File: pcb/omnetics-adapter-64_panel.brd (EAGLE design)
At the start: 119 x 83 mm, 87 parts, among them J1 DF40-REC, J10 DF40-REC, J13 DF40-REC, J16 DF40-REC, J19 DF40-REC, J22 DF40-REC, J25 DF40-REC, J4 DF40-REC, J7 DF40-REC

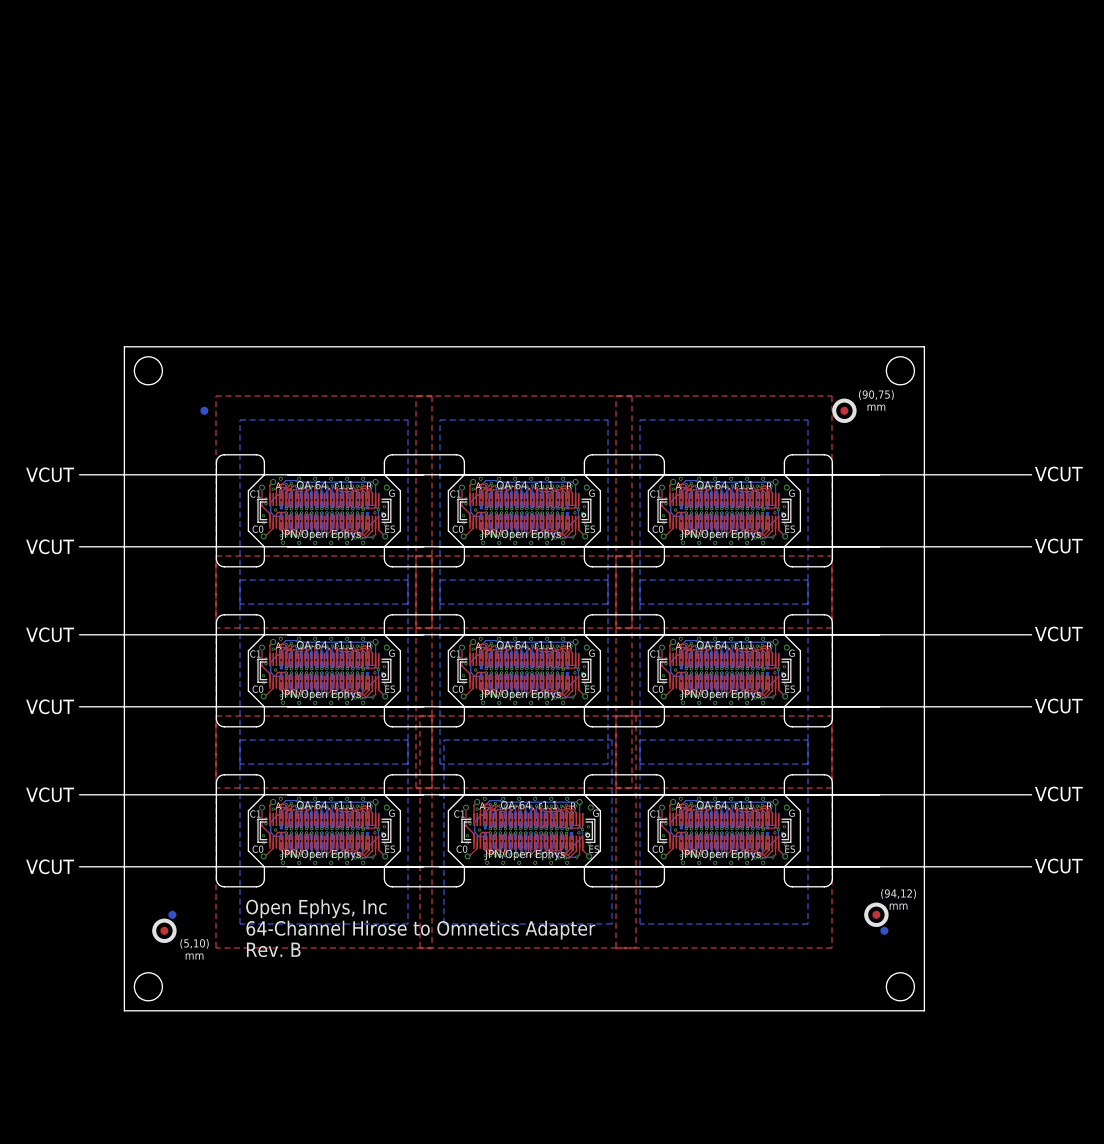
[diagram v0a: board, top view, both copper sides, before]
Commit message: Replace design with 1.3 pinout
- This pinout fits headstage-64 that is in the field
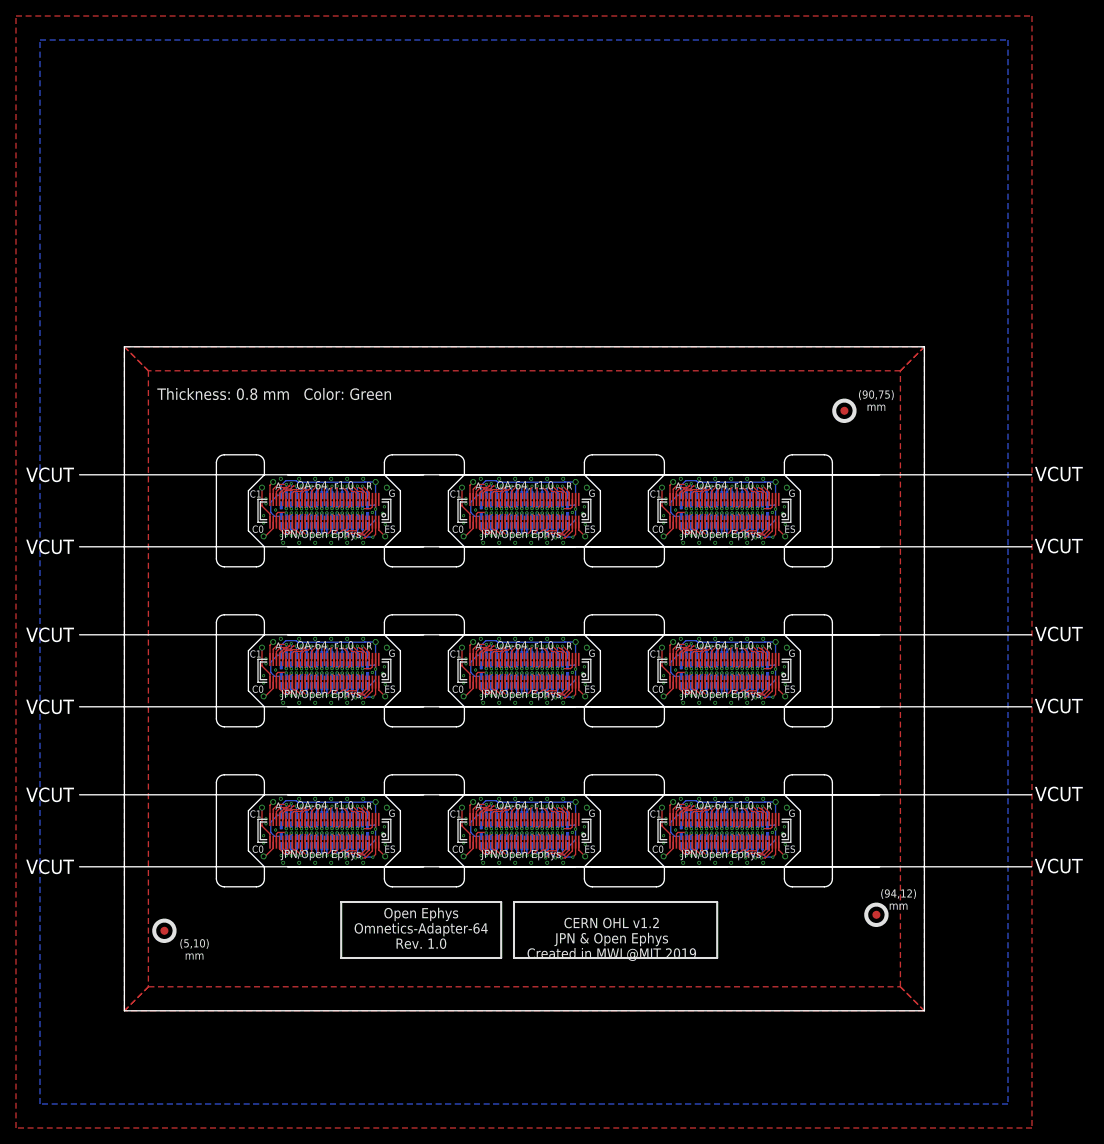
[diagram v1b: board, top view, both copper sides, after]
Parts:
- removed E$4, E$5, E$6: (no value), fiducial:FIDUCIAL
- moved CAT12 50.0 mm to (17.4, 59.3)
- moved CAT16 50.0 mm to (67.4, 59.3)
- moved ESTIM19 50.0 mm to (31.4, 66.1)
- moved ESTIM25 50.0 mm to (81.4, 66.1)
- moved CAT13 50.0 mm to (17.2, 65.4)
- moved CAT17 50.0 mm to (67.2, 65.4)
- moved ESTIM20 50.0 mm to (32.8, 65.4)
- moved ESTIM26 50.0 mm to (82.8, 65.4)
- moved J19 50.0 mm to (25.0, 62.5)
- moved J25 50.0 mm to (75.0, 62.5)
- moved AN6 50.0 mm to (18.6, 66.1)
- moved AN8 50.0 mm to (68.6, 66.1)
- moved ESTIM18 50.0 mm to (32.6, 59.3)
- moved ESTIM24 50.0 mm to (82.6, 59.3)
- moved J20 50.0 mm to (19.6, 64.5)
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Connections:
- removed net GND1: ESTIM2.P$1, J1.37, J2.18, J2.36, J3.18, J3.36
- removed net GND2: ESTIM8.P$1, J7.37, J8.18, J8.36, J9.18, J9.36
- removed net GND3: ESTIM11.P$1, J10.37, J11.18, J11.36, J12.18, J12.36
- removed net GND4: ESTIM14.P$1, J13.37, J14.18, J14.36, J15.18, J15.36
- removed net GND5: ESTIM17.P$1, J16.37, J17.18, J17.36, J18.18, J18.36
- removed net GND6: ESTIM20.P$1, J19.37, J20.18, J20.36, J21.18, J21.36
- removed net GND7: ESTIM23.P$1, J22.37, J23.18, J23.36, J24.18, J24.36
- removed net GND8: ESTIM26.P$1, J25.37, J26.18, J26.36, J27.18, J27.36
- net GND: now also ESTIM11.P$1, ESTIM14.P$1, ESTIM17.P$1, ESTIM2.P$1, ESTIM20.P$1, ESTIM23.P$1, ESTIM26.P$1, ESTIM8.P$1, J1.70, J10.70, J11.18, J11.36, J12.18, J12.36, J13.70, J14.18, J14.36, J15.18, J15.36, J16.70, J17.18, J17.36, J18.18, J18.36, J19.70, J2.18, J2.36, J20.18, J20.36, J21.18, J21.36, J22.70, J23.18, J23.36, J24.18, J24.36, J25.70, J26.18, J26.36, J27.18, J27.36, J3.18, J3.36, J4.70, J7.70, J8.18, J8.36, J9.18, J9.36; no longer J4.37
- net N$1: now also J1.68; no longer J1.69
- net N$100: now also J4.37; no longer J4.38
- net N$12: now also J1.57; no longer J1.60
- net N$129: now also J7.68; no longer J7.69
- net N$130: now also J7.66; no longer J7.67
- net N$131: now also J7.64; no longer J7.65
- net N$132: now also J7.63; no longer J7.64
- net N$133: now also J7.62; no longer J7.63
- net N$135: now also J7.60; no longer J7.62
- net N$138: now also J7.57; no longer J7.60
- net N$14: now also J1.55; no longer J1.57
- net N$140: now also J7.55; no longer J7.57
- net N$142: now also J7.53; no longer J7.55
- net N$143: now also J7.52; no longer J7.53
- net N$144: now also J7.51; no longer J7.52
- net N$145: now also J7.50; no longer J7.51
- net N$146: now also J7.49; no longer J7.50
- net N$147: now also J7.48; no longer J7.49
- net N$148: now also J7.47; no longer J7.48
- net N$149: now also J7.46; no longer J7.47
- net N$150: now also J7.45; no longer J7.46
- net N$151: now also J7.44; no longer J7.45
- net N$152: now also J7.43; no longer J7.44
- net N$153: now also J7.42; no longer J7.43
- net N$154: now also J7.41; no longer J7.42
- net N$155: now also J7.40; no longer J7.41
- net N$156: now also J7.38; no longer J7.39
- net N$16: now also J1.53; no longer J1.55
- net N$161: now also J7.65; no longer J7.66
- net N$162: now also J7.67; no longer J7.68
- net N$163: now also J7.39; no longer J7.40
- net N$164: now also J7.37; no longer J7.38
- net N$17: now also J1.52; no longer J1.53
- net N$18: now also J1.51; no longer J1.52
- net N$19: now also J1.50; no longer J1.51
- net N$193: now also J10.68; no longer J10.69
- net N$194: now also J10.66; no longer J10.67
- net N$195: now also J10.64; no longer J10.65
- net N$196: now also J10.63; no longer J10.64
- net N$197: now also J10.62; no longer J10.63
- net N$199: now also J10.60; no longer J10.62
- net N$2: now also J1.65; no longer J1.66
- net N$20: now also J1.49; no longer J1.50
- net N$21: now also J1.48; no longer J1.49
- net N$22: now also J1.47; no longer J1.48
- net N$229: now also J10.57; no longer J10.60
- net N$23: now also J1.46; no longer J1.47
- net N$231: now also J10.55; no longer J10.57
- net N$233: now also J10.53; no longer J10.55
- net N$234: now also J10.52; no longer J10.53
- net N$235: now also J10.51; no longer J10.52
- net N$236: now also J10.50; no longer J10.51
- net N$237: now also J10.49; no longer J10.50
- net N$238: now also J10.48; no longer J10.49
- net N$239: now also J10.47; no longer J10.48
- net N$24: now also J1.45; no longer J1.46
- net N$240: now also J10.46; no longer J10.47
- net N$241: now also J10.45; no longer J10.46
- net N$242: now also J10.44; no longer J10.45
- net N$243: now also J10.43; no longer J10.44
- net N$244: now also J10.42; no longer J10.43
- net N$245: now also J10.41; no longer J10.42
- net N$246: now also J10.40; no longer J10.41
- net N$247: now also J10.38; no longer J10.39
- net N$25: now also J1.44; no longer J1.45
- net N$252: now also J10.65; no longer J10.66
- net N$253: now also J10.67; no longer J10.68
- net N$254: now also J10.39; no longer J10.40
- net N$255: now also J10.37; no longer J10.38
- net N$26: now also J1.43; no longer J1.44
- net N$27: now also J1.42; no longer J1.43
- net N$28: now also J1.41; no longer J1.42
- net N$284: now also J13.68; no longer J13.69
- net N$285: now also J13.66; no longer J13.67
- net N$286: now also J13.64; no longer J13.65
- net N$287: now also J13.63; no longer J13.64
- net N$288: now also J13.62; no longer J13.63
- net N$29: now also J1.40; no longer J1.41
- net N$290: now also J13.60; no longer J13.62
- net N$293: now also J13.57; no longer J13.60
- net N$295: now also J13.55; no longer J13.57
- net N$297: now also J13.53; no longer J13.55
- net N$298: now also J13.52; no longer J13.53
- net N$299: now also J13.51; no longer J13.52
- net N$3: now also J1.66; no longer J1.67
- net N$30: now also J1.39; no longer J1.40
- net N$300: now also J13.50; no longer J13.51
- net N$301: now also J13.49; no longer J13.50
- net N$302: now also J13.48; no longer J13.49
- net N$303: now also J13.47; no longer J13.48
- net N$304: now also J13.46; no longer J13.47
- net N$305: now also J13.45; no longer J13.46
- net N$306: now also J13.44; no longer J13.45
- net N$307: now also J13.43; no longer J13.44
- net N$308: now also J13.42; no longer J13.43
- net N$309: now also J13.41; no longer J13.42
- net N$31: now also J1.38; no longer J1.39
- net N$310: now also J13.40; no longer J13.41
- net N$311: now also J13.38; no longer J13.39
- net N$316: now also J13.65; no longer J13.66
- net N$317: now also J13.67; no longer J13.68
- net N$318: now also J13.39; no longer J13.40
- net N$319: now also J13.37; no longer J13.38
- net N$32: now also J1.37; no longer J1.38
- net N$348: now also J16.68; no longer J16.69
- net N$349: now also J16.66; no longer J16.67
- net N$350: now also J16.64; no longer J16.65
- net N$351: now also J16.63; no longer J16.64
- net N$352: now also J16.62; no longer J16.63
- net N$354: now also J16.60; no longer J16.62
- net N$357: now also J16.57; no longer J16.60
- net N$359: now also J16.55; no longer J16.57
- net N$361: now also J16.53; no longer J16.55
- net N$362: now also J16.52; no longer J16.53
- net N$363: now also J16.51; no longer J16.52
- net N$364: now also J16.50; no longer J16.51
- net N$365: now also J16.49; no longer J16.50
- net N$366: now also J16.48; no longer J16.49
- net N$367: now also J16.47; no longer J16.48
- net N$368: now also J16.46; no longer J16.47
- net N$369: now also J16.45; no longer J16.46
- net N$370: now also J16.44; no longer J16.45
- net N$371: now also J16.43; no longer J16.44
- net N$372: now also J16.42; no longer J16.43
- net N$373: now also J16.41; no longer J16.42
- net N$374: now also J16.40; no longer J16.41
- net N$375: now also J16.38; no longer J16.39
- net N$380: now also J16.65; no longer J16.66
- net N$381: now also J16.67; no longer J16.68
- net N$382: now also J16.39; no longer J16.40
- net N$383: now also J16.37; no longer J16.38
- net N$4: now also J1.67; no longer J1.68
- net N$412: now also J19.68; no longer J19.69
- net N$413: now also J19.66; no longer J19.67
- net N$414: now also J19.64; no longer J19.65
- net N$415: now also J19.63; no longer J19.64
- net N$416: now also J19.62; no longer J19.63
- net N$418: now also J19.60; no longer J19.62
- net N$421: now also J19.57; no longer J19.60
- net N$423: now also J19.55; no longer J19.57
- net N$425: now also J19.53; no longer J19.55
- net N$426: now also J19.52; no longer J19.53
- net N$427: now also J19.51; no longer J19.52
- net N$428: now also J19.50; no longer J19.51
- net N$429: now also J19.49; no longer J19.50
- net N$430: now also J19.48; no longer J19.49
- net N$431: now also J19.47; no longer J19.48
- net N$432: now also J19.46; no longer J19.47
- net N$433: now also J19.45; no longer J19.46
- net N$434: now also J19.44; no longer J19.45
- net N$435: now also J19.43; no longer J19.44
- net N$436: now also J19.42; no longer J19.43
- net N$437: now also J19.41; no longer J19.42
- net N$438: now also J19.40; no longer J19.41
- net N$439: now also J19.38; no longer J19.39
- net N$444: now also J19.65; no longer J19.66
- net N$445: now also J19.67; no longer J19.68
- net N$446: now also J19.39; no longer J19.40
- net N$447: now also J19.37; no longer J19.38
- net N$476: now also J22.68; no longer J22.69
- net N$477: now also J22.66; no longer J22.67
- net N$478: now also J22.64; no longer J22.65
- net N$479: now also J22.63; no longer J22.64
- net N$480: now also J22.62; no longer J22.63
- net N$482: now also J22.60; no longer J22.62
- net N$485: now also J22.57; no longer J22.60
- net N$487: now also J22.55; no longer J22.57
- net N$489: now also J22.53; no longer J22.55
- net N$490: now also J22.52; no longer J22.53
- net N$491: now also J22.51; no longer J22.52
- net N$492: now also J22.50; no longer J22.51
- net N$493: now also J22.49; no longer J22.50
- net N$494: now also J22.48; no longer J22.49
- net N$495: now also J22.47; no longer J22.48
- net N$496: now also J22.46; no longer J22.47
- net N$497: now also J22.45; no longer J22.46
- net N$498: now also J22.44; no longer J22.45
- net N$499: now also J22.43; no longer J22.44
- net N$5: now also J1.64; no longer J1.65
- net N$500: now also J22.42; no longer J22.43
- net N$501: now also J22.41; no longer J22.42
- net N$502: now also J22.40; no longer J22.41
- net N$503: now also J22.38; no longer J22.39
- net N$508: now also J22.65; no longer J22.66
- net N$509: now also J22.67; no longer J22.68
- net N$510: now also J22.39; no longer J22.40
- net N$511: now also J22.37; no longer J22.38
- net N$540: now also J25.68; no longer J25.69
- net N$541: now also J25.66; no longer J25.67
- net N$542: now also J25.64; no longer J25.65
- net N$543: now also J25.63; no longer J25.64
- net N$544: now also J25.62; no longer J25.63
- net N$546: now also J25.60; no longer J25.62
- net N$549: now also J25.57; no longer J25.60
- net N$551: now also J25.55; no longer J25.57
- net N$553: now also J25.53; no longer J25.55
- net N$554: now also J25.52; no longer J25.53
- net N$555: now also J25.51; no longer J25.52
- net N$556: now also J25.50; no longer J25.51
- net N$557: now also J25.49; no longer J25.50
- net N$558: now also J25.48; no longer J25.49
- net N$559: now also J25.47; no longer J25.48
- net N$560: now also J25.46; no longer J25.47
- net N$561: now also J25.45; no longer J25.46
- net N$562: now also J25.44; no longer J25.45
- net N$563: now also J25.43; no longer J25.44
- net N$564: now also J25.42; no longer J25.43
- net N$565: now also J25.41; no longer J25.42
- net N$566: now also J25.40; no longer J25.41
- net N$567: now also J25.38; no longer J25.39
- net N$572: now also J25.65; no longer J25.66
- net N$573: now also J25.67; no longer J25.68
- net N$574: now also J25.39; no longer J25.40
- net N$575: now also J25.37; no longer J25.38
- net N$6: now also J1.63; no longer J1.64
- net N$65: now also J4.68; no longer J4.69
- net N$66: now also J4.66; no longer J4.67
- net N$67: now also J4.64; no longer J4.65
- net N$68: now also J4.63; no longer J4.64
- net N$69: now also J4.62; no longer J4.63
- net N$7: now also J1.62; no longer J1.63
- net N$71: now also J4.60; no longer J4.62
- net N$74: now also J4.57; no longer J4.60
- net N$76: now also J4.55; no longer J4.57
- net N$78: now also J4.53; no longer J4.55
- net N$79: now also J4.52; no longer J4.53
- net N$80: now also J4.51; no longer J4.52
- net N$81: now also J4.50; no longer J4.51
- net N$82: now also J4.49; no longer J4.50
- net N$83: now also J4.48; no longer J4.49
- net N$84: now also J4.47; no longer J4.48
- net N$85: now also J4.46; no longer J4.47
- net N$86: now also J4.45; no longer J4.46
- net N$87: now also J4.44; no longer J4.45
- net N$88: now also J4.43; no longer J4.44
- net N$89: now also J4.42; no longer J4.43
- net N$9: now also J1.60; no longer J1.62
- net N$90: now also J4.41; no longer J4.42
- net N$91: now also J4.40; no longer J4.41
- net N$92: now also J4.38; no longer J4.39
- net N$97: now also J4.65; no longer J4.66
- net N$98: now also J4.67; no longer J4.68
- net N$99: now also J4.39; no longer J4.40
- net REF: now also J1.69; no longer J1.70
- net REF1: now also J4.69; no longer J4.70
- net REF2: now also J7.69; no longer J7.70
- net REF3: now also J10.69; no longer J10.70
- net REF4: now also J13.69; no longer J13.70
- net REF5: now also J16.69; no longer J16.70
- net REF6: now also J19.69; no longer J19.70
- net REF7: now also J22.69; no longer J22.70
- net REF8: now also J25.69; no longer J25.70
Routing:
- net N$437: track 1.73 -> 3.48 mm
- net N$90: track 1.73 -> 3.48 mm
- net N$373: track 1.73 -> 3.48 mm
- net N$154: track 1.73 -> 3.48 mm
- net N$28: track 1.73 -> 3.48 mm
- net N$565: track 1.73 -> 3.48 mm
- net N$501: track 1.73 -> 3.48 mm
- net N$245: track 1.73 -> 3.48 mm
- net N$309: track 1.73 -> 3.48 mm
- net N$241: track 1.59 -> 2.81 mm
- net N$561: track 1.59 -> 2.81 mm
- net N$305: track 1.59 -> 2.81 mm
- net N$497: track 1.59 -> 2.81 mm
- net N$369: track 1.59 -> 2.81 mm
- net N$150: track 1.59 -> 2.81 mm
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- added copper zone on layer 1, net S$1
- added copper zone on layer 1, net S$2
- added copper zone on layer 1, net S$3
- added copper zone on layer 1, net S$4
- removed copper zone on layer 1, net GND1
- removed copper zone on layer 16, net GND1
- removed copper zone on layer 1, net GND2
- removed copper zone on layer 16, net GND2
- removed copper zone on layer 1, net GND3
- removed copper zone on layer 16, net GND3
- removed copper zone on layer 1, net GND4
- removed copper zone on layer 16, net GND4
- removed copper zone on layer 1, net GND5
- removed copper zone on layer 16, net GND5
- removed copper zone on layer 1, net GND6
- removed copper zone on layer 16, net GND6
- removed copper zone on layer 1, net GND7
- removed copper zone on layer 16, net GND7
- removed copper zone on layer 1, net GND8
- removed copper zone on layer 16, net GND8
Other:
- outline, holes or cut-outs redrawn
- board text added: "CERN OHL v1.2 JPN & Open Ephys Created in MWL@MIT 2019"
- board text added: "OA-64, r1.0"
- board text added: "Open Ephys Omnetics-Adapter-64 Rev. 1.0"
- board text added: "Thickness: 0.8 mm Color: Green"
- board text removed: "OA-64, r1.1"
- board text removed: "Open Ephys, Inc 64-Channel Hirose to Omnetics Adapter Rev. B"
